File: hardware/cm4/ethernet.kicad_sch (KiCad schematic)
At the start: 5 parts, among them J14 HR911105A, U12 TPD4EUSB30

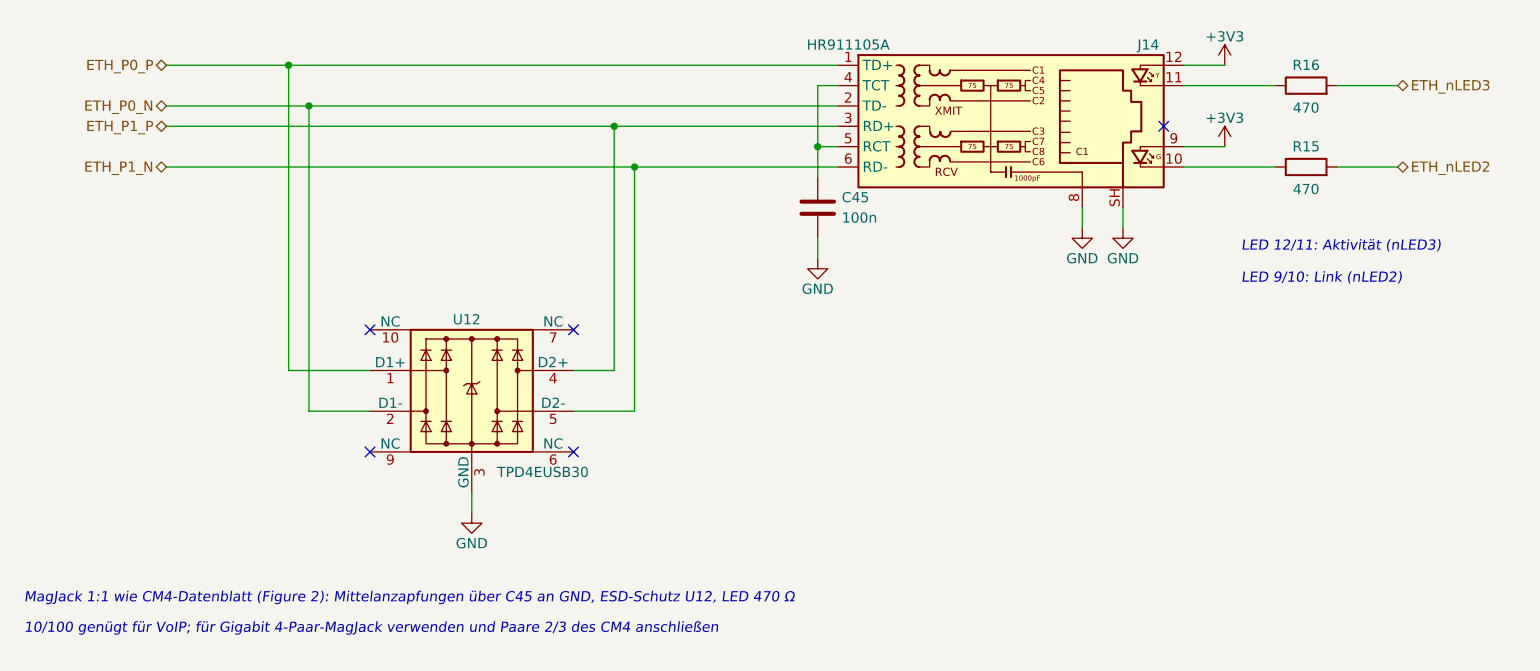
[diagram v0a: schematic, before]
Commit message: CM4-Träger 0.3: Leiterplatte (4 Lagen, JLCPCB), Ein/Aus-Taster, Lüfter, lieferbare Teile
Schaltplan
- Codec TI TLV320AIC3204 statt WM8731 (abgekündigt); MCLK 12 MHz, Reset GPIO26, I²C an GPIO0/1
- Ein/Aus-Taster an GPIO3 (gpio-shutdown im Betrieb, Bootloader-Wecken im Halt)
- Lüfterblatt: AO3400A an GPIO12, Freilaufdiode, JST-PH-Anschluss; gpio-fan über SoC-Temperatur
- Konfig-Taster SW2 und Status-LED D3; Würth RJ45/RJ12, Bourns SM-LP-5001, TPD4E05U06
- reproduzierbare UUIDs (Schaltplan ↔ Platine bleiben verknüpft), eigene Footprints in hardware/bibliothek

Leiterplatte (erzeuge_layout.py)
- 110 × 85 mm, F.Cu / In1 GND / In2 +3V3 / B.Cu, JLC04161H-7628, JLCPCB-Regeln (.kicad_dru)
- CM4-Lage nach CM4IO-Referenz, Antennen-Sperrzone, isolierte Bereiche GND_ISO/GNDA mit Trennstreifen
- eigenes Fanout zu den Ebenen, Routing mit FreeRouting 1.9.0 über xvfb (2.x: Telemetrie an)
- DRC ohne Verstöße, 0 offene Verbindungen, Schaltplan ↔ Platine identisch
- Bestellliste für Digikey mit geprüftem Lagerbestand
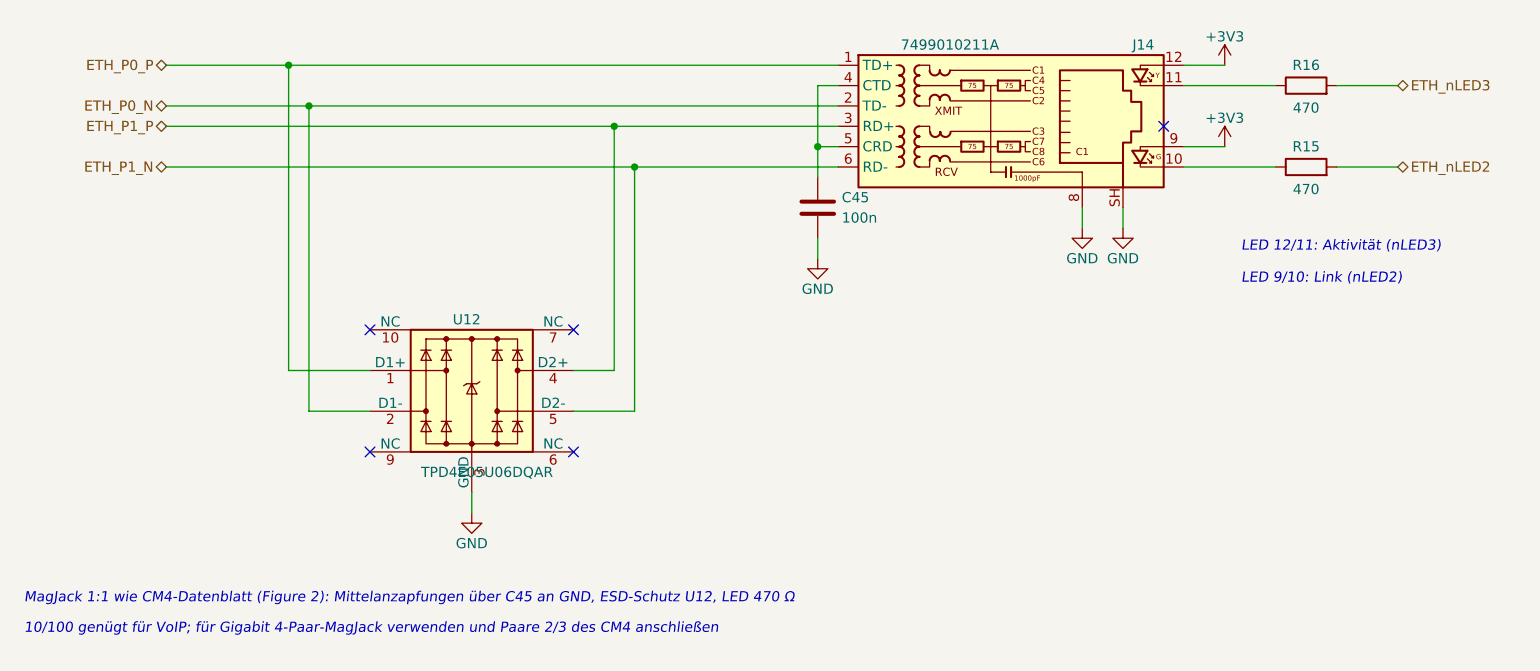
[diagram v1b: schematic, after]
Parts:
- removed J14: HR911105A, Connector_RJ:RJ45_Hanrun_HR911105A_Horizontal, symbol Connector:RJ45_Hanrun_HR911105A_Horizontal
- removed U12: TPD4EUSB30, Package_SON:USON-10_2.5x1.0mm_P0.5mm, symbol Power_Protection:TPD4EUSB30
- added J14: 7499010211A, Connector_RJ:RJ45_Wuerth_7499010211A_Horizontal, symbol Connector:RJ45_Wuerth_7499010211A
- added U12: TPD4E05U06DQAR, Package_SON:USON-10_2.5x1.0mm_P0.5mm, symbol Power_Protection:TPD4E05U06DQA
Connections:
- net +3V3: now also J14.12, J14.9
- net ETH_P0_N: now also J14.2 (TD-), U12.2 (D1-)
- net ETH_P0_P: now also J14.1 (TD+), U12.1 (D1+)
- net ETH_P1_N: now also J14.6 (RD-), U12.5 (D2-)
- net ETH_P1_P: now also J14.3 (RD+), U12.4 (D2+)
- net GND: now also J14.8, J14.SH, U12.3 (GND), U12.8 (GND)
- net at R15.1: now also J14.10
- net at R16.1: now also J14.11
- net at C45.1: now also J14.4 (CTD), J14.5 (CRD)
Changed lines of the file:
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@@
 	)
 	(symbol
-		(lib_id "Connector:RJ45_Hanrun_HR911105A_Horizontal")
+		(lib_id "Connector:RJ45_Wuerth_7499010211A")
 		(at 240.03 106.68 0)
 		(unit 1)
@@
 		(dnp no)
 		(property "Reference" "J14"
-			(at 258.44 96.52 0)
-			(effects (font (size 1.27 1.27)))
-		)
-		(property "Value" "HR911105A"
-			(at 220.98 96.52 0)
-			(effects (font (size 1.27 1.27)))
-		)
-		(property "Footprint" "Connector_RJ:RJ45_Hanrun_HR911105A_Horizontal"
+			(at 257.81 96.52 0)
+			(effects (font (size 1.27 1.27)))
+		)
+		(property "Value" "7499010211A"
+			(at 233.68 96.52 0)
+			(effects (font (size 1.27 1.27)))
+		)
+		(property "Footprint" "Connector_RJ:RJ45_Wuerth_7499010211A_Horizontal"
 			(at 240.03 106.68 0)
 			(effects (font (size 1.27 1.27)) (hide yes))
@@
 		(instances
 			(project "sopho2sip-cm4"
-				(path "/4a9740d4-98df-4f49-9691-e6a39846794f/42f5ee7a-c3ac-4787-8301-92de14f14410" (reference "J14") (unit 1))
+				(path "/c325dfb5-e80f-5288-9c1c-dd309ced8908/f43193ea-a65d-5b2d-9a13-25ee6eb2cb77" (reference "J14") (unit 1))
 			)
 		)
@@
 		(instances
 			(project "sopho2sip-cm4"
-				(path "/4a9740d4-98df-4f49-9691-e6a39846794f/42f5ee7a-c3ac-4787-8301-92de14f14410" (reference "C45") (unit 1))
-			)
-		)
-	)
-	(symbol
-		(lib_id "Power_Protection:TPD4EUSB30")
+				(path "/c325dfb5-e80f-5288-9c1c-dd309ced8908/f43193ea-a65d-5b2d-9a13-25ee6eb2cb77" (reference "C45") (unit 1))
+			)
+		)
+	)
+	(symbol
+		(lib_id "Power_Protection:TPD4E05U06DQA")
 		(at 173.99 139.7 0)
 		(unit 1)
@@
 			(effects (font (size 1.27 1.27)))
 		)
-		(property "Value" "TPD4EUSB30"
-			(at 182.88 149.86 0)
+		(property "Value" "TPD4E05U06DQAR"
+			(at 175.9 149.86 0)
 			(effects (font (size 1.27 1.27)))
 		)
@@
 		(instances
 			(project "sopho2sip-cm4"
-				(path "/4a9740d4-98df-4f49-9691-e6a39846794f/42f5ee7a-c3ac-4787-8301-92de14f14410" (reference "U12") (unit 1))
+				(path "/c325dfb5-e80f-5288-9c1c-dd309ced8908/f43193ea-a65d-5b2d-9a13-25ee6eb2cb77" (reference "U12") (unit 1))
 			)
 		)
@@
 		(instances
 			(project "sopho2sip-cm4"
-				(path "/4a9740d4-98df-4f49-9691-e6a39846794f/42f5ee7a-c3ac-4787-8301-92de14f14410" (reference "R16") (unit 1))
+				(path "/c325dfb5-e80f-5288-9c1c-dd309ced8908/f43193ea-a65d-5b2d-9a13-25ee6eb2cb77" (reference "R16") (unit 1))
 			)
 		)
@@
 		(instances
 			(project "sopho2sip-cm4"
-				(path "/4a9740d4-98df-4f49-9691-e6a39846794f/42f5ee7a-c3ac-4787-8301-92de14f14410" (reference "R15") (unit 1))
+				(path "/c325dfb5-e80f-5288-9c1c-dd309ced8908/f43193ea-a65d-5b2d-9a13-25ee6eb2cb77" (reference "R15") (unit 1))
 			)
 		)
@@
 		(instances
 			(project "sopho2sip-cm4"
-				(path "/4a9740d4-98df-4f49-9691-e6a39846794f/42f5ee7a-c3ac-4787-8301-92de14f14410" (reference "#PWRETH001") (unit 1))
+				(path "/c325dfb5-e80f-5288-9c1c-dd309ced8908/f43193ea-a65d-5b2d-9a13-25ee6eb2cb77" (reference "#PWRETH001") (unit 1))
 			)
 		)
@@
 		(instances
 			(project "sopho2sip-cm4"
-				(path "/4a9740d4-98df-4f49-9691-e6a39846794f/42f5ee7a-c3ac-4787-8301-92de14f14410" (reference "#PWRETH002") (unit 1))
+				(path "/c325dfb5-e80f-5288-9c1c-dd309ced8908/f43193ea-a65d-5b2d-9a13-25ee6eb2cb77" (reference "#PWRETH002") (unit 1))
 			)
 		)
@@
 		(instances
 			(project "sopho2sip-cm4"
-				(path "/4a9740d4-98df-4f49-9691-e6a39846794f/42f5ee7a-c3ac-4787-8301-92de14f14410" (reference "#PWRETH003") (unit 1))
+				(path "/c325dfb5-e80f-5288-9c1c-dd309ced8908/f43193ea-a65d-5b2d-9a13-25ee6eb2cb77" (reference "#PWRETH003") (unit 1))
 			)
 		)
@@
 		(instances
 			(project "sopho2sip-cm4"
-				(path "/4a9740d4-98df-4f49-9691-e6a39846794f/42f5ee7a-c3ac-4787-8301-92de14f14410" (reference "#PWRETH004") (unit 1))
+				(path "/c325dfb5-e80f-5288-9c1c-dd309ced8908/f43193ea-a65d-5b2d-9a13-25ee6eb2cb77" (reference "#PWRETH004") (unit 1))
 			)
 		)
@@
 		(instances
 			(project "sopho2sip-cm4"
-				(path "/4a9740d4-98df-4f49-9691-e6a39846794f/42f5ee7a-c3ac-4787-8301-92de14f14410" (reference "#PWRETH005") (unit 1))
+				(path "/c325dfb5-e80f-5288-9c1c-dd309ced8908/f43193ea-a65d-5b2d-9a13-25ee6eb2cb77" (reference "#PWRETH005") (unit 1))
 			)
 		)
@@
 		(instances
 			(project "sopho2sip-cm4"
-				(path "/4a9740d4-98df-4f49-9691-e6a39846794f/42f5ee7a-c3ac-4787-8301-92de14f14410" (reference "#PWRETH006") (unit 1))
-			)
-		)
+				(path "/c325dfb5-e80f-5288-9c1c-dd309ced8908/f43193ea-a65d-5b2d-9a13-25ee6eb2cb77" (reference "#PWRETH006") (unit 1))
+			)
+		)

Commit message: Schaltplan: Hinweise als Textkästen (KiCad bricht um); Texte werden in den Generator zurückgeführt
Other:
- note removed: "10/100 genügt für VoIP; für Gigabit 4-Paar-MagJack verwenden und Paare 2/3 des CM4 anschließen"
- note removed: "MagJack 1:1 wie CM4-Datenblatt (Figure 2): Mittelanzapfungen über C45 an GND, ESD-Schutz U12, LED 470 Ω"
- moved on the sheet: C45, J14, R15, R16, U12

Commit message: CM4-Schaltplan: Handänderungen übernommen (Handlage für 8 Blätter, 2 Texte zurückgeführt); Kastenhöhen aus gemessenen Zeichenbreiten
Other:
- moved on the sheet: C45, J14, R15, R16, U12
